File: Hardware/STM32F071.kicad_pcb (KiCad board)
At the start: 2 copper layers, 50 x 50 mm, 13 parts, among them J1 USB_C_Receptacle_USB2.0_16P, U1 STM32C071K8Tx, U2 USBLC6-2P6, U4 XL1509-ADJE1

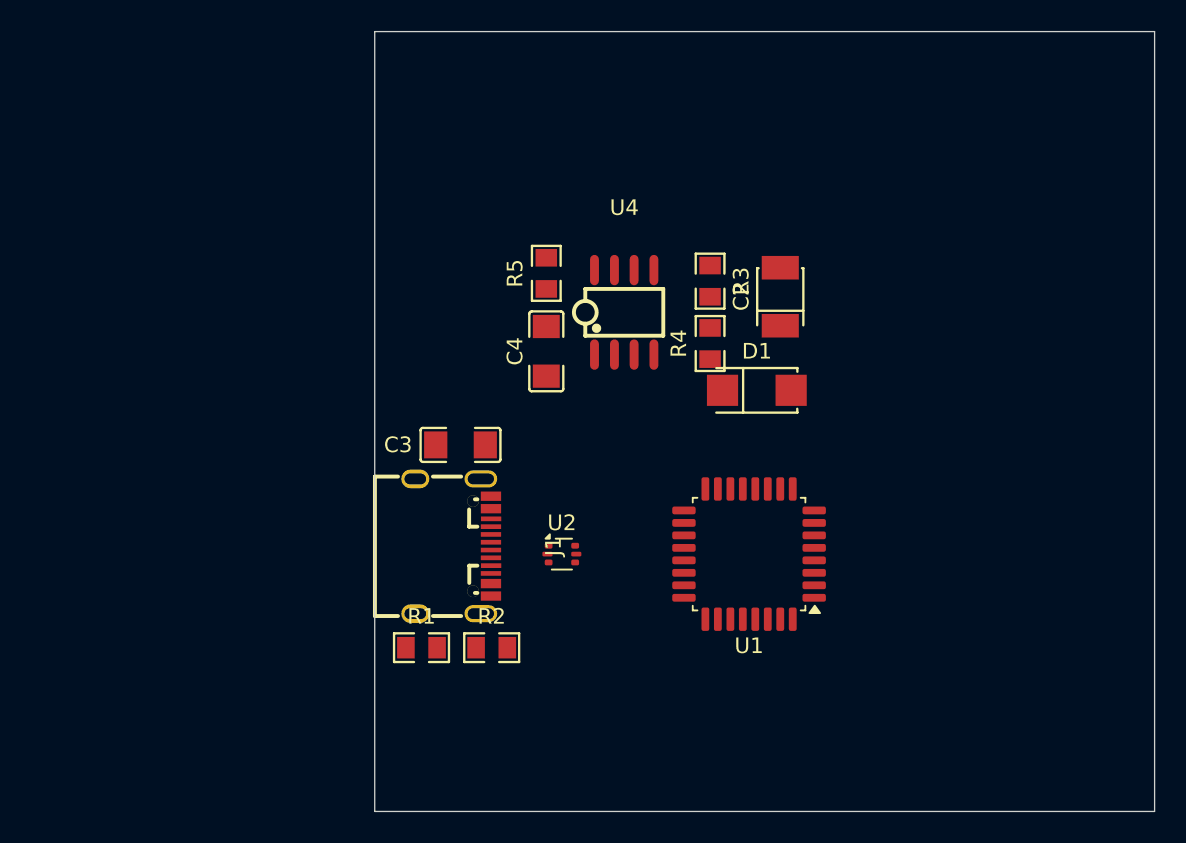
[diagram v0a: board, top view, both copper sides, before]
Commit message: New Power supply and USB connector laid out
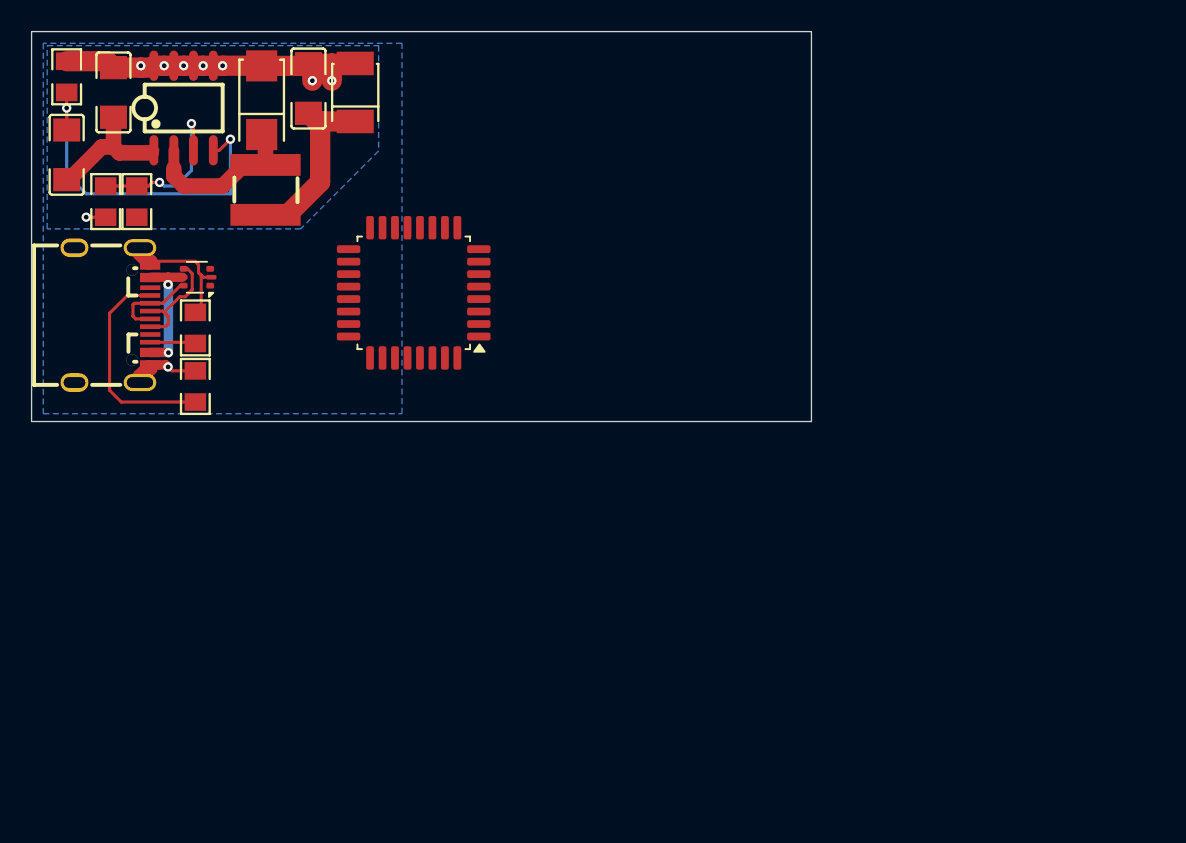
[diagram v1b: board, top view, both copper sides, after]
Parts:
- added C5: 10uF, jlcbasic:C1206, F.Cu at (117.8, 78.7)
- added L1: 100uH, project:IND-SMD_L4.0-W4.0_SMNR4030, F.Cu at (115.0, 85.2)
- moved R3 39.1 mm to (104.8, 85.9), turned to 90 degrees
- moved R4 37.9 mm to (106.8, 85.9), turned to -90 degrees
- moved D1 36.8 mm to (114.8, 79.4), turned to 90 degrees
- moved C4 33.2 mm to (102.2, 82.9)
- moved R5 33.2 mm to (102.2, 77.9)
- moved C3 31.7 mm to (105.2, 78.9), turned to -90 degrees
- moved U4 31.1 mm to (109.8, 79.9)
- moved C2 30.2 mm to (120.8, 78.9)
- moved U2 29.4 mm to (110.6, 90.8), turned to 180 degrees
- moved U1 27.3 mm to (124.5, 91.8)
- moved J1 26.4 mm to (105.2, 93.2)
- moved R2 25.3 mm to (110.5, 97.8), turned to 90 degrees
- moved R1 25.1 mm to (110.5, 94.0), turned to -90 degrees
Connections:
- J1 pad 0: (no net) -> GND
- U2 pad 1: Net-(J1-D--PadA7) -> Net-(U1-PA11)
- U2 pad 3: Net-(J1-D+-PadA6) -> Net-(U1-PA12)
- U2 pad 4: Net-(U1-PA12) -> Net-(J1-D+-PadA6)
- U2 pad 6: Net-(U1-PA11) -> Net-(J1-D--PadA7)
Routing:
- net GND: track 0.00 -> 35.1 mm, vias 0 -> 9
- net Net-(U4-ON/OFF): track 0.00 -> 23.3 mm, vias 0 -> 2
- net VBUS: track 0.00 -> 16.7 mm, vias 0 -> 2
- net Net-(J1-CC1): track 0.00 -> 13.8 mm
- net +3.3V: track 0.00 -> 11.4 mm
- net Net-(U4-FB): track 0.00 -> 11.4 mm, vias 0 -> 2
- net Net-(D1-K): track 0.00 -> 10.6 mm
- net Net-(J1-D+-PadA6): track 0.00 -> 7.47 mm
- net Net-(J1-D--PadA7): track 0.00 -> 5.67 mm
- net Net-(J1-CC2): track 0.00 -> 2.93 mm
- added copper zone on B.Cu, net GND
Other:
- board size 50 x 50 mm -> 50 x 25 mm
